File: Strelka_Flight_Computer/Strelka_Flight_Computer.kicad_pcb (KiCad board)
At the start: 4 copper layers, 91 x 30.1 mm, 170 parts, among them IC1 XTSD04GLGEAG, IC2 MAX-M10S-00B, J1 1S_LiPo_LARGE_HOLE_XT-30, J2 SM04B-GHS-TB(LF)(SN)-, J3 DB125-3.5-4P-GN-S, J4 SM06B-GHS-TB(LF)(SN), J6 USB_B_Micro, Q1 CJK2333, Q10 AP2300, Q11 MMBT2222, Q2 CJK2333, Q3 AO3401A, Q4 AO3401A, Q5 AP2300, Q6 MMBT2222, Q8 AO3401A, Q9 AO3401A, SW1 SW_Push, SW2 SW_Push, SW3 SM02B-GHS-TB(LF)(SN), U10 LM321, U11 BMX055, U12 MS561101BA03-50, U15 LM321, U16 TPS61085DGKR, U2 AP9101CK6, U3 AMS1117-3.3, U4 RFM95W-915S2, U5 STM32F405RGTx, U8 USBLC6-2SC6, Y1 Q13FC1350000200, Y2 X322524MOB4SI

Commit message: Started design for V2
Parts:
- removed C12: 0.1uF, Capacitor_SMD:C_0603_1608Metric_Pad1.08x0.95mm_HandSolder
- removed C13: 100nF, Capacitor_SMD:C_0603_1608Metric_Pad1.08x0.95mm_HandSolder
- removed C14, C16: 2.2uF, Capacitor_SMD:C_0603_1608Metric_Pad1.08x0.95mm_HandSolder
- removed C15: 10uF, Capacitor_SMD:C_0603_1608Metric_Pad1.08x0.95mm_HandSolder
- removed C17, C18: 10nF, Capacitor_SMD:C_0603_1608Metric_Pad1.08x0.95mm_HandSolder
- removed C19, C20: 8pF, Capacitor_SMD:C_0603_1608Metric_Pad1.08x0.95mm_HandSolder
- removed C2: 1u, Capacitor_SMD:C_0603_1608Metric
- removed C21, C22: 18pF, Capacitor_SMD:C_0603_1608Metric_Pad1.08x0.95mm_HandSolder
- removed C3: 10n, Capacitor_SMD:C_0603_1608Metric
- removed C4: 2.2u, Capacitor_SMD:C_0603_1608Metric
- removed C49, C50, C52, C53, C54: NC, Capacitor_SMD:C_0603_1608Metric
- removed D9: 1SS388, Diode_SMD:D_SOD-523
- removed FB1: BLM18PG221SN1D, Inductor_SMD:L_0603_1608Metric
- removed G***: LOGO, Footprints:Strelka_Logo
- removed G***: LOGO, Footprints:HPR_Logo
- removed I1, I2: AL5809-30S1-7, Diode_SMD:D_SOD-123
- removed J1: 1S_LiPo_LARGE_HOLE_XT-30, Connector_AMASS:AMASS_XT30PW-M_1x02_P2.50mm_Horizontal
- removed JP2: UART_Switch, Footprints:UART_Switch
- removed Q3, Q8: AO3401A, Package_TO_SOT_SMD:SOT-23
- removed R16, R17, R18, R19: 0, Resistor_SMD:R_0603_1608Metric_Pad0.98x0.95mm_HandSolder
- removed R22, R25: 10k, Resistor_SMD:R_0603_1608Metric_Pad0.98x0.95mm_HandSolder
- removed R28, R34, R48, R54: 1k, Resistor_SMD:R_0603_1608Metric
- removed R32, R52, R64, R69: 100k, Resistor_SMD:R_0603_1608Metric
- removed SW2: SW_Push, Button_Switch_SMD:SW_Push_SPST_NO_Alps_SKRK
- removed SW3: SM02B-GHS-TB(LF)(SN), Footprints:SM02BGHSTBLFSN
- removed U10, U15: LM321, Package_TO_SOT_SMD:SOT-23-5
- removed Y1: Q13FC1350000200, Crystal:Crystal_SMD_3215-2Pin_3.2x1.5mm
- removed Y2: X322524MOB4SI, Crystal:Crystal_SMD_3225-4Pin_3.2x2.5mm
- added BZ1: Buzzer, Footprints:HNB09A05, F.Cu at (102.3, 110.0)
- added C23: 100n, Capacitor_SMD:C_0402_1005Metric, F.Cu at (120.2, 107.8)
- added C24: 100n, Capacitor_SMD:C_0402_1005Metric, F.Cu at (120.2, 109.7)
- added C25: 100n, Capacitor_SMD:C_0402_1005Metric, F.Cu at (120.2, 111.7)
- added C32: 100n, Capacitor_SMD:C_0402_1005Metric, F.Cu at (120.2, 113.7)
- added C33: 100n, Capacitor_SMD:C_0402_1005Metric, F.Cu at (123.1, 105.8)
- added C34: 1u, Capacitor_SMD:C_0402_1005Metric, F.Cu at (123.1, 107.8)
- added C35: 2.2u, Capacitor_SMD:C_0402_1005Metric, F.Cu at (123.1, 109.7)
- added C42: 2.2u, Capacitor_SMD:C_0402_1005Metric, F.Cu at (123.1, 111.7)
- added C43: 100n, Capacitor_SMD:C_0402_1005Metric, F.Cu at (123.1, 113.7)
- added C44: 18p, Capacitor_SMD:C_0402_1005Metric, F.Cu at (125.9, 105.8)
- added C45: 18p, Capacitor_SMD:C_0402_1005Metric, F.Cu at (125.9, 107.8)
- added C5: 100n, Capacitor_SMD:C_0402_1005Metric, F.Cu at (120.2, 105.8)
- added C58: 18p, Capacitor_SMD:C_0402_1005Metric, F.Cu at (125.9, 109.7)
- added C59: 18p, Capacitor_SMD:C_0402_1005Metric, F.Cu at (125.9, 111.7)
- added D15: RED LED, LED_SMD:LED_0603_1608Metric, F.Cu at (126.7, 101.1)
- added D7: BLUE LED, LED_SMD:LED_0603_1608Metric, F.Cu at (126.7, 95.9)
- added D8: YELLOW LED, LED_SMD:LED_0603_1608Metric, F.Cu at (126.7, 98.5)
- added J5: Conn_01x07, Footprints:SM05B-GHS-TBLFSN, F.Cu at (189.1, 66.2)
- added J7: Conn_01x02, Footprints:MOLEX_43045-0200, F.Cu at (105.0, 52.0)
- added JP1: Jumper_2_Bridged, Jumper:SolderJumper-2_P1.3mm_Bridged_Pad1.0x1.5mm, F.Cu at (130.9, 96.4)
- added JP3: Jumper_2_Bridged, Jumper:SolderJumper-2_P1.3mm_Bridged_Pad1.0x1.5mm, F.Cu at (130.9, 99.9)
- added JP4: UART_Switch, Footprints:UART_Switch, F.Cu at (75.0, 158.0)
- added L1: 10u, Inductor_SMD:L_0805_2012Metric, F.Cu at (106.9, 116.6)
- added Q12: AO3400A, Package_TO_SOT_SMD:SOT-23, F.Cu at (129.8, 111.5)
- added Q13: AO3401A, Package_TO_SOT_SMD:SOT-23, F.Cu at (129.8, 115.9)
- added Q7: AO3400A, Package_TO_SOT_SMD:SOT-23, F.Cu at (129.8, 107.0)
- added R1: 100k, Resistor_SMD:R_0402_1005Metric, F.Cu at (111.5, 105.8)
- added R2: 1k, Resistor_SMD:R_0402_1005Metric, F.Cu at (111.5, 107.8)
- added R23: 1k, Resistor_SMD:R_0402_1005Metric, F.Cu at (114.4, 109.8)
- added R26: 10k, Resistor_SMD:R_0402_1005Metric, F.Cu at (114.4, 111.8)
- added R4: 10k, Resistor_SMD:R_0402_1005Metric, F.Cu at (111.5, 109.8)
- added R41: 0R, Resistor_SMD:R_0402_1005Metric, F.Cu at (114.4, 113.8)
- added R44: 10k, Resistor_SMD:R_0402_1005Metric, F.Cu at (117.3, 105.8)
- added R45: 10k, Resistor_SMD:R_0402_1005Metric, F.Cu at (117.3, 107.8)
- added R46: 1k, Resistor_SMD:R_0402_1005Metric, F.Cu at (117.3, 109.8)
- added R5: 33R, Resistor_SMD:R_0402_1005Metric, F.Cu at (111.5, 111.8)
- added R6: 1k, Resistor_SMD:R_0402_1005Metric, F.Cu at (111.5, 113.8)
- added R70: 100k, Resistor_SMD:R_0402_1005Metric, F.Cu at (117.3, 111.8)
- added R71: NC, Resistor_SMD:R_0603_1608Metric_Pad0.98x0.95mm_HandSolder, F.Cu at (112.2, 116.0)
- added R72: 10k, Resistor_SMD:R_0603_1608Metric_Pad0.98x0.95mm_HandSolder, F.Cu at (112.2, 118.5)
- added SW4: TS-1185-C-A-A-A, Button_Switch_SMD:SW_Push_SPST_NO_Alps_SKRK, F.Cu at (121.4, 96.8)
- added SW5: TS-1185-C-A-A-A, Button_Switch_SMD:SW_Push_SPST_NO_Alps_SKRK, F.Cu at (121.4, 101.3)
- added TP1: TestPoint, TestPoint:TestPoint_Pad_1.0x1.0mm, F.Cu at (95.9, 112.8)
- added TP11: TestPoint, TestPoint:TestPoint_Pad_1.0x1.0mm, F.Cu at (136.7, 162.2)
- added TP2: TestPoint, TestPoint:TestPoint_Pad_1.0x1.0mm, F.Cu at (127.5, 159.2)
- added U1: STM32F407VGTx, Package_QFP:LQFP-100_14x14mm_P0.5mm, F.Cu at (150.0, 66.2)
- added Y3: Q13FC1350000400, Crystal:Crystal_SMD_3215-2Pin_3.2x1.5mm, F.Cu at (140.5, 126.7)
- added Y4: X322524MOB4SI, Crystal:Crystal_SMD_3225-4Pin_3.2x2.5mm, F.Cu at (143.0, 130.5)
- AE1: footprint Connector_Coaxial:SMA_Amphenol_132134_Vertical -> Footprints:STA-10201
- AE2: footprint Connector_Coaxial:U.FL_Hirose_U.FL-R-SMT-1_Vertical -> Footprints:STA-10201
- BT2, C28, C29, C30, C31, C36, C38, C46, C47, C48, C51, C55, C56, C57, C6, D1, D11, D14, L2, MOSFET1, Q1, Q11, Q6, R27, R3, R30, R31, R35, R36, R37, R38, R39, R40, R47, R49, R53, R56, R61, R62, R63, R7, R9, U11, U12, U16, U2, U4, U8: moved to F.Cu
- C1: value 2.2u -> 100n; footprint Capacitor_SMD:C_0603_1608Metric -> Capacitor_SMD:C_0402_1005Metric
- D3: value E6X0602QBAC1UDA -> BZT52C3V6T; footprint LED_SMD:LED_0603_1608Metric_Pad1.05x0.95mm_HandSolder -> Diode_SMD:D_SOD-523
- D5: value 1SS388 -> BZT52C3V6T; moved to F.Cu
- J2: value SM04B-GHS-TB(LF)(SN)- -> Conn_01x04
- R10: value 10k -> 10R; footprint Resistor_SMD:R_0603_1608Metric -> Resistor_SMD:R_0402_1005Metric
- R11: footprint Resistor_SMD:R_0603_1608Metric -> Resistor_SMD:R_0402_1005Metric
- R12: value 10R -> 1k; footprint Resistor_SMD:R_0603_1608Metric -> Resistor_SMD:R_0402_1005Metric
- R13: value 200R -> 120R; footprint Resistor_SMD:R_0603_1608Metric_Pad0.98x0.95mm_HandSolder -> Resistor_SMD:R_0402_1005Metric
- R14, R15: value 0 -> 10k; footprint Resistor_SMD:R_0603_1608Metric_Pad0.98x0.95mm_HandSolder -> Resistor_SMD:R_0603_1608Metric; moved to F.Cu
- R21: value 10k -> 1k; footprint Resistor_SMD:R_0603_1608Metric_Pad0.98x0.95mm_HandSolder -> Resistor_SMD:R_0603_1608Metric; moved to F.Cu
- R24: value NC -> 1k; footprint Resistor_SMD:R_0603_1608Metric_Pad0.98x0.95mm_HandSolder -> Resistor_SMD:R_0603_1608Metric
- SW1: value SW_Push -> SW_DIP_x01; footprint Button_Switch_SMD:SW_Push_SPST_NO_Alps_SKRK -> Footprints:MOLEX_43045-0200
- U5: value STM32F405RGTx -> MCP2551-I-SN; footprint Package_QFP:LQFP-64_10x10mm_P0.5mm -> Package_SO:SOIC-8_3.9x4.9mm_P1.27mm
- moved J2 135.8 mm to (63.4, 156.9), turned to 0 degrees
- moved J6 131.1 mm to (63.3, 162.9), turned to 0 degrees
- moved U8 116.6 mm to (70.9, 154.7), turned to 0 degrees
- moved R12 109.7 mm to (75.0, 153.5), turned to 0 degrees
- moved U5 109.1 mm to (72.4, 163.1)
- moved R56 108.5 mm to (81.9, 134.8)
- moved C39 105.3 mm to (81.9, 129.8), turned to 0 degrees
- moved C40 104.8 mm to (81.9, 132.3), turned to 0 degrees
- moved C38 104.6 mm to (81.9, 127.3)
- moved BT2 104.3 mm to (88.1, 140.9), turned to 0 degrees
- moved R58 100.9 mm to (81.9, 139.9), turned to 0 degrees
- moved C11 100.8 mm to (69.9, 144.9), turned to 0 degrees
- moved R57 98.4 mm to (81.9, 137.3), turned to 0 degrees
- moved R40 98.3 mm to (108.4, 163.9), turned to 0 degrees
- moved C10 97.9 mm to (69.9, 142.3), turned to 0 degrees
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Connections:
- C1 pad 1: GND -> +5V
- C1 pad 2: Net-(C1-Pad2) -> GND
- D1 pad 1: Net-(D1-Pad1) -> Net-(D1-K)
- D3 pad 1: Net-(D3-Pad1) -> /Actuators/DROGUE_CONT
- D3 pad 2: /STM32F405/INDICATOR_LED -> GND
- D5 pad 1: /Actuators/Ematch_Drogue1/EMATCH+ -> /Actuators/MAIN_CONT
- D5 pad 2: Net-(D5-Pad2) -> GND
- IC2 pad 16: /STM32F405/I2C2_SDA -> /STM32F407/I2C2_SDA
- IC2 pad 17: /STM32F405/I2C2_SCL -> /STM32F407/I2C2_SCL
- IC2 pad 2: Net-(IC2-Pad2) -> /STM32F407/USART2_RX
- IC2 pad 3: Net-(IC2-Pad3) -> /STM32F407/USART2_TX
- IC2 pad 9: /STM32F405/GPIO_PA10 -> /STM32F407/GPIO_PA10
- J2 pad 1: /Data_Interfaces/SWCLK -> GND
- J2 pad 2: /Data_Interfaces/SWDIO -> /Data_Interfaces/CAN_+
- J2 pad 3: GND -> /Data_Interfaces/CAN_-
- J2 pad 4: +3V3 -> GND
- J2 pad SH1: GND -> (no net)
- J2 pad SH2: GND -> (no net)
- Q1 pad 2: Net-(D1-Pad1) -> Net-(D1-K)
- R10 pad 1: Net-(R10-Pad1) -> Net-(U1-PB14)
- R10 pad 2: GND -> /Data_Interfaces/USB_D-
- R11 pad 1: /Data_Interfaces/USB_D- -> Net-(U1-PB15)
- R11 pad 2: /STM32F405/USB2_IN- -> /Data_Interfaces/USB_D+
- R12 pad 1: /Data_Interfaces/USB_D+ -> Net-(U5-Rs)
- R12 pad 2: /STM32F405/USB2_IN+ -> GND
- R13 pad 1: GND -> /Data_Interfaces/CAN_+
- R13 pad 2: Net-(D3-Pad1) -> /Data_Interfaces/CAN_-
- R14 pad 1: /Data_Logging/SD0 -> /Actuators/DROGUE_CONT
- R14 pad 2: /STM32F405/SDIO_D0 -> /Actuators/Ematch_Drogue1/EMATCH+
- R15 pad 1: /Data_Logging/SD1 -> /Actuators/MAIN_CONT
- R15 pad 2: /STM32F405/SDIO_D1 -> /Actuators/Ematch_Main/EMATCH+
- R21 pad 1: /STM32F405/I2C2_SDA -> /Actuators/Ematch_Drogue1/EMATCH+
- R21 pad 2: +3V3 -> VDC
- R24 pad 1: /STM32F405/SD_DET -> /Actuators/Ematch_Main/EMATCH+
- R24 pad 2: +3V3 -> VDC
- R58 pad 2: /STM32F405/GPIO_PB7 -> /STM32F407/GPIO_PB7
- SW1 pad 1: +3V3 -> Net-(D1-K)
- SW1 pad 2: Net-(R10-Pad1) -> VDC
- TP10 pad 1: /STM32F405/USART2_TX -> /STM32F407/USART2_TX
- TP5 pad 1: /Actuators/DROGUE_CONT -> /STM32F407/SPI2_NSS3
- TP6 pad 1: /STM32F405/SPI2_MOSI -> /915MHz_Radio/SPI_MOSI
- TP7 pad 1: /STM32F405/SPI2_MISO -> /915MHz_Radio/SPI_MISO
- TP8 pad 1: /STM32F405/SPI2_SCK -> /915MHz_Radio/SPI_CLK
- TP9 pad 1: /STM32F405/USART2_RX -> /STM32F407/USART2_RX
- U11 pad 11: /STM32F405/SPI2_MOSI -> /915MHz_Radio/SPI_MOSI
- U11 pad 12: /STM32F405/SPI2_MISO -> /915MHz_Radio/SPI_MISO
- U11 pad 14: /STM32F405/INT_IN2 -> /STM32F407/INT_IN2
- U11 pad 16: /STM32F405/SPI2_NSS2 -> /STM32F407/SPI2_NSS2
- U11 pad 17: /STM32F405/SPI2_MISO -> /915MHz_Radio/SPI_MISO
- U11 pad 19: /STM32F405/INT_IN1 -> /STM32F407/INT_IN1
- U11 pad 2: /STM32F405/INT_IN3 -> /STM32F407/INT_IN3
- U11 pad 20: /STM32F405/SPI2_NSS4 -> /STM32F407/SPI2_NSS4
- U11 pad 5: /STM32F405/SPI2_NSS3 -> /STM32F407/SPI2_NSS3
- U11 pad 9: /STM32F405/SPI2_SCK -> /915MHz_Radio/SPI_CLK
- U12 pad 4: /STM32F405/SPI2_NSS1 -> /STM32F407/SPI2_NSS1
- U12 pad 5: /STM32F405/SPI2_NSS1 -> /STM32F407/SPI2_NSS1
- U12 pad 6: /STM32F405/SPI2_MISO -> /STM32F407/SPI2_MISO
- U12 pad 7: /STM32F405/SPI2_MOSI -> /STM32F407/SPI2_MOSI
- U12 pad 8: /STM32F405/SPI2_SCK -> /STM32F407/SPI2_SCK
- U5 pad 1: +3V3 -> Net-(JP4-RX1)
- U5 pad 2: /Actuators/CONT_TEST_EN -> GND
- U5 pad 3: /STM32F405/OSC32_IN -> +5V
- U5 pad 4: /STM32F405/OSC32_OUT -> Net-(JP4-TX1)
- U5 pad 5: /STM32F405/OSC_IN -> unconnected-(U5-Vref-Pad5)
- U5 pad 6: /STM32F405/OSC_OUT -> /Data_Interfaces/CAN_-
- U5 pad 7: Net-(C12-Pad2) -> /Data_Interfaces/CAN_+
- U5 pad 8: /Power/BATT_VOLT -> Net-(U5-Rs)
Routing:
- net +3V3: track 159.9 -> 0.00 mm, vias 41 -> 0
- net GND: track 102.2 -> 0.00 mm, vias 48 -> 0
- net VDC: track 90.5 -> 0.00 mm, vias 5 -> 0
- net /Actuators/CONT_TEST_EN: track 66.1 -> 0.00 mm, vias 5 -> 0
- net VBUS: track 64.9 -> 0.00 mm, vias 3 -> 0
- net /Actuators/DROGUE_CONT: track 62.4 -> 0.00 mm, vias 2 -> 0
- net Net-(C12-Pad2): track 56.9 -> 0.00 mm, vias 2 -> 0
- net /Actuators/MAIN_CONT: track 55.8 -> 0.00 mm, vias 2 -> 0
- net /Actuators/DROGUE_L: track 54.0 -> 0.00 mm, vias 4 -> 0
- net /STM32F405/USART2_TX: track 50.7 -> 0.00 mm, vias 2 -> 0
- net /STM32F405/SPI2_MISO: track 50.4 -> 0.00 mm, vias 5 -> 0
- net /Data_Interfaces/SWCLK: track 48.5 -> 0.00 mm, vias 2 -> 0
- net /STM32F405/SPI2_MOSI: track 46.1 -> 0.00 mm, vias 5 -> 0
- net Net-(R10-Pad1): track 45.4 -> 0.00 mm, vias 2 -> 0
- net /Actuators/MAIN_L: track 44.5 -> 0.00 mm, vias 4 -> 0
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- removed copper zone on F.Cu, net +3V3
- removed copper zone on In2.Cu, net +3V3
- removed copper zone on B.Cu, net GND
- removed copper zone on F.Cu, net GND
- removed copper zone on In1.Cu, net GND
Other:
- board size 91 x 30.1 mm -> 93.7 x 35.8 mm
- board text removed: "+"
- board text removed: "+3.3V"
- board text removed: "+5V"
- board text removed: "-"
- board text removed: "4.2Vin MAX"
- board text removed: "BOOT"
- board text removed: "Batt PWR Select"
- board text removed: "DROGUE"
- board text removed: "Designed by Angus McLennan Nov 2022"
- board text removed: "GPS"
- board text removed: "JLCJLCJLC"
- board text removed: "MAIN"
- board text removed: "MISO"
- board text removed: "MOSI"
- board text removed: "MS5611"
- board text removed: "PWR SW"
- board text removed: "RST"
- board text removed: "RX2"
- board text removed: "SCK"
- board text removed: "SWD"
- board text removed: "TX2"
- board text removed: "UART SW"

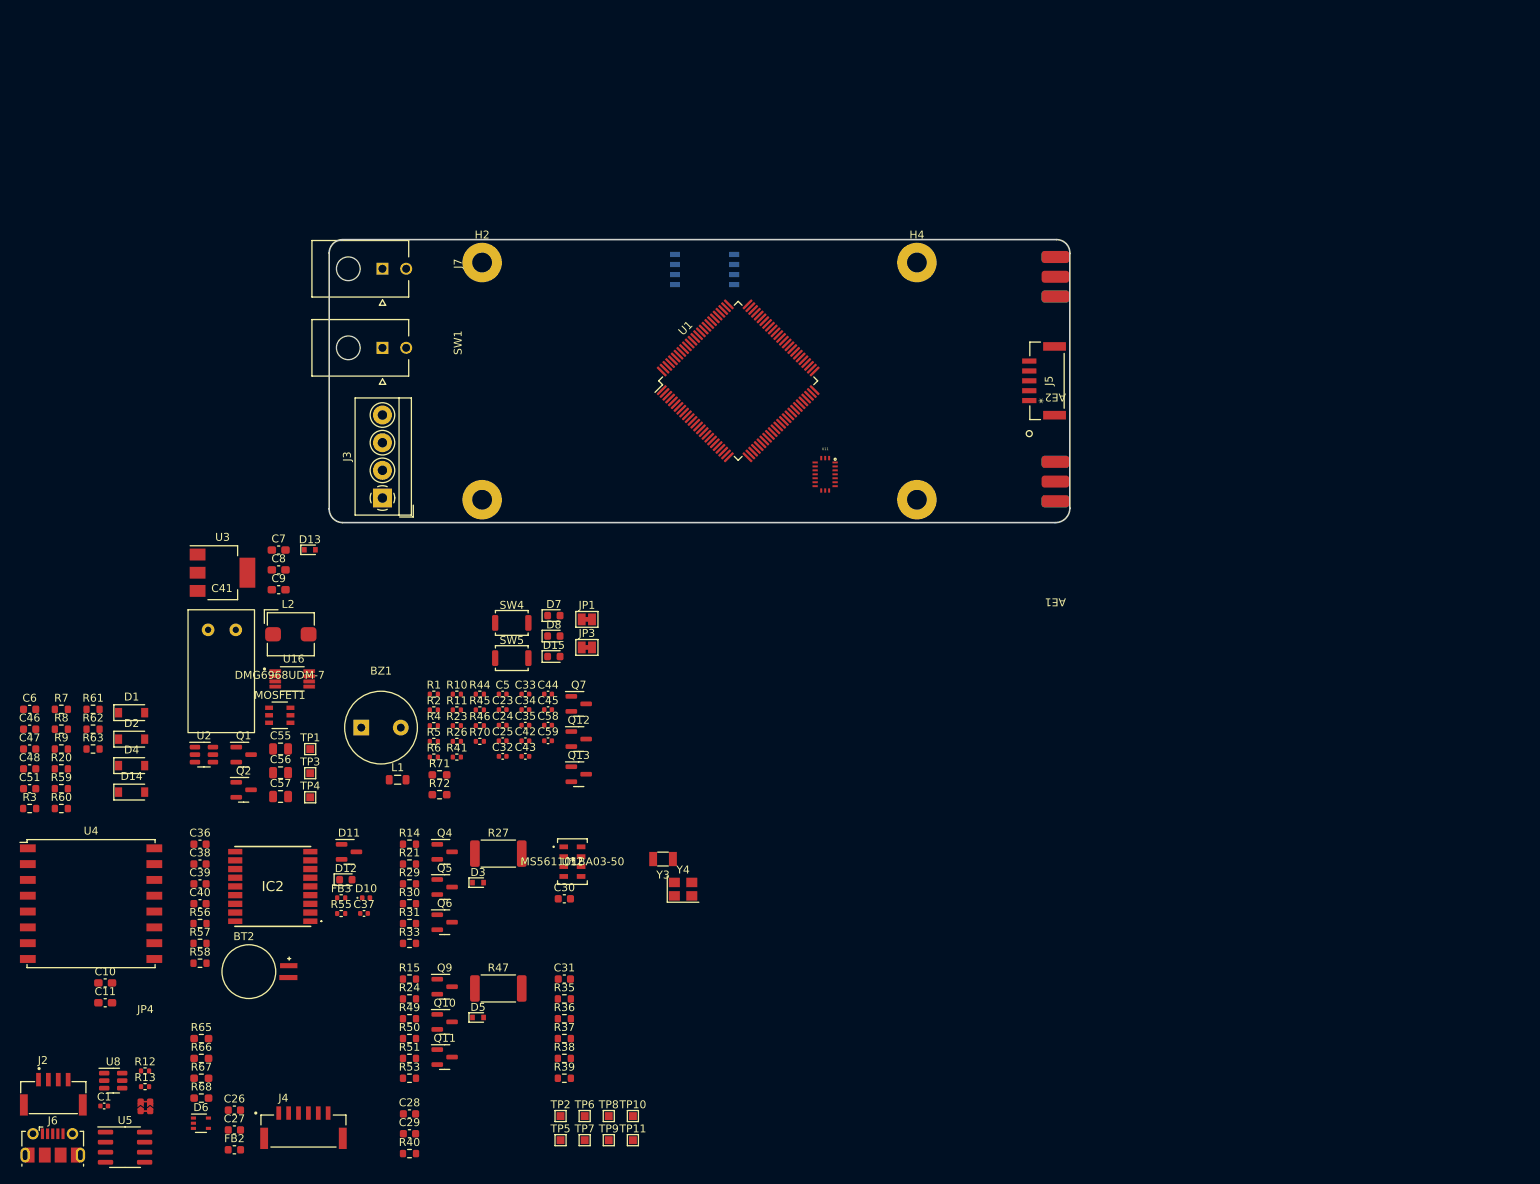
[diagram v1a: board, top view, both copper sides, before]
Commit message: Changes main processor to h4745
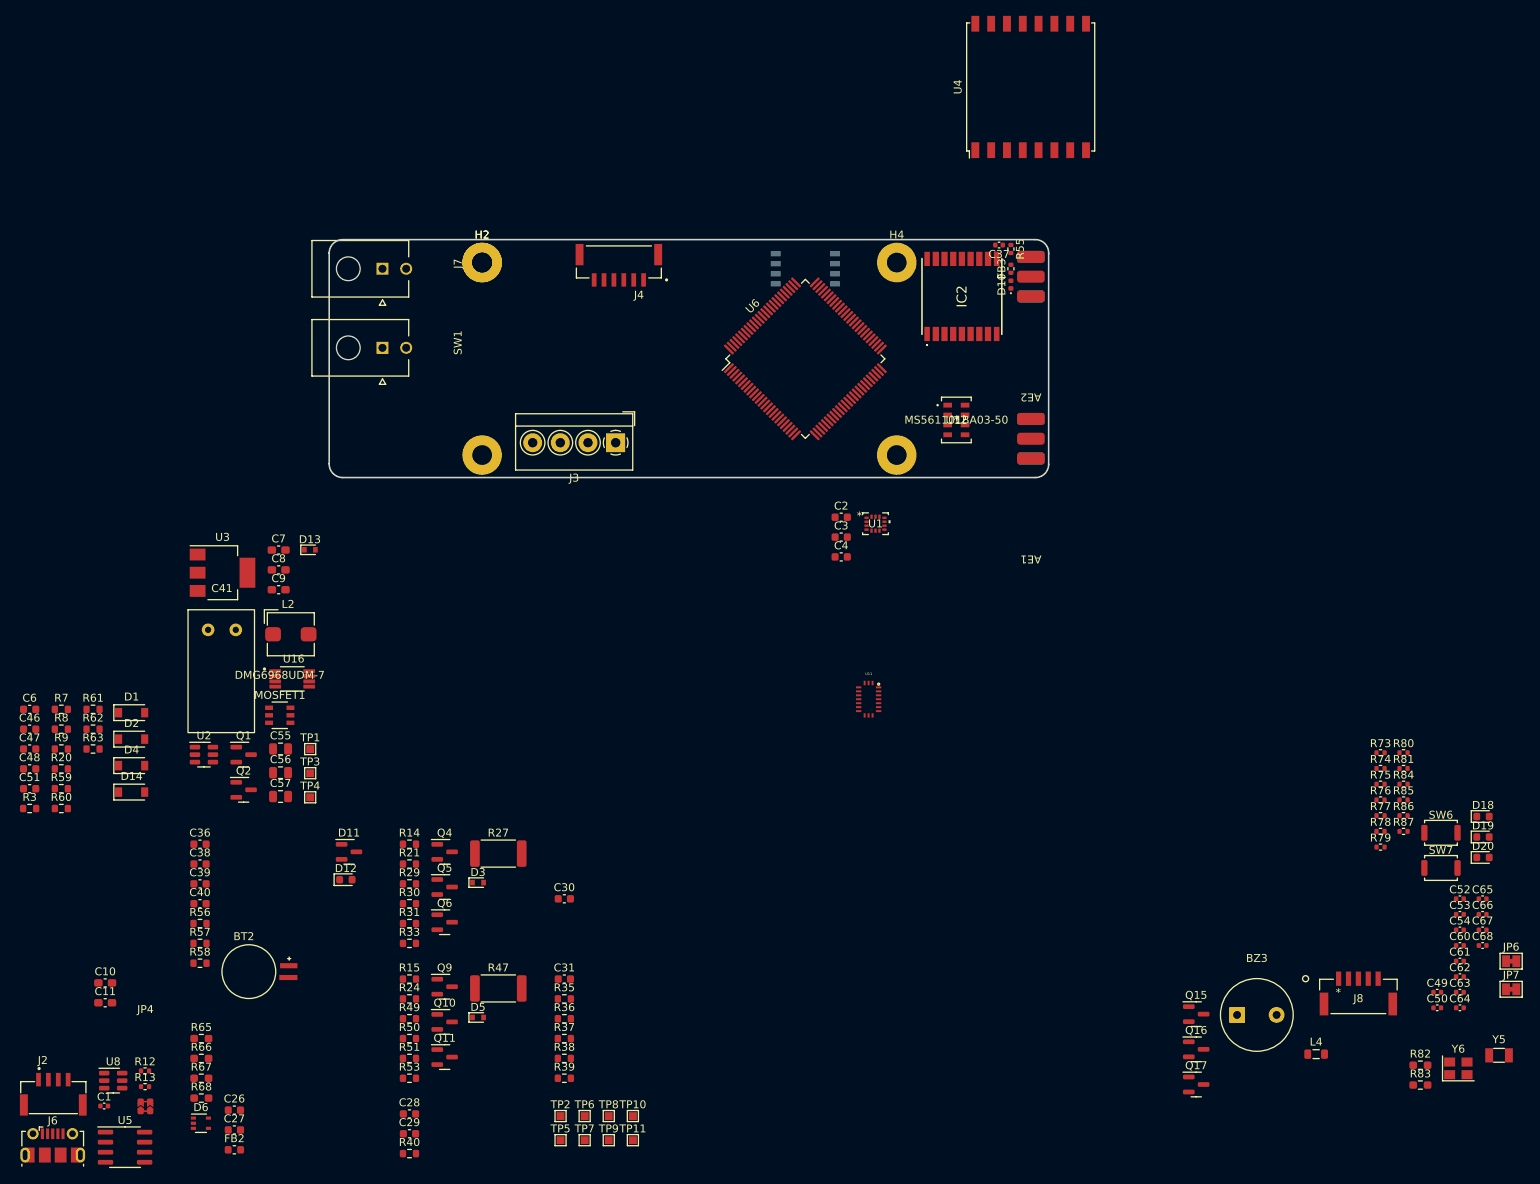
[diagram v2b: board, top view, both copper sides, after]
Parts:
- removed BZ1: Buzzer, Footprints:HNB09A05
- removed C23, C24, C25, C32, C33, C43, C5: 100n, Capacitor_SMD:C_0402_1005Metric
- removed C34: 1u, Capacitor_SMD:C_0402_1005Metric
- removed C35, C42: 2.2u, Capacitor_SMD:C_0402_1005Metric
- removed C44, C45, C58, C59: 18p, Capacitor_SMD:C_0402_1005Metric
- removed D15: RED LED, LED_SMD:LED_0603_1608Metric
- removed D7: BLUE LED, LED_SMD:LED_0603_1608Metric
- removed D8: YELLOW LED, LED_SMD:LED_0603_1608Metric
- removed J5: Conn_01x07, Footprints:SM05B-GHS-TBLFSN
- removed JP1, JP3: Jumper_2_Bridged, Jumper:SolderJumper-2_P1.3mm_Bridged_Pad1.0x1.5mm
- removed L1: 10u, Inductor_SMD:L_0805_2012Metric
- removed Q12, Q7: AO3400A, Package_TO_SOT_SMD:SOT-23
- removed Q13: AO3401A, Package_TO_SOT_SMD:SOT-23
- removed R1, R70: 100k, Resistor_SMD:R_0402_1005Metric
- removed R10, R11: 10R, Resistor_SMD:R_0402_1005Metric
- removed R2, R23, R46, R6: 1k, Resistor_SMD:R_0402_1005Metric
- removed R26, R4, R44, R45: 10k, Resistor_SMD:R_0402_1005Metric
- removed R41: 0R, Resistor_SMD:R_0402_1005Metric
- removed R5: 33R, Resistor_SMD:R_0402_1005Metric
- removed R71: NC, Resistor_SMD:R_0603_1608Metric_Pad0.98x0.95mm_HandSolder
- removed R72: 10k, Resistor_SMD:R_0603_1608Metric_Pad0.98x0.95mm_HandSolder
- removed SW4, SW5: TS-1185-C-A-A-A, Button_Switch_SMD:SW_Push_SPST_NO_Alps_SKRK
- removed Y3: Q13FC1350000400, Crystal:Crystal_SMD_3215-2Pin_3.2x1.5mm
- removed Y4: X322524MOB4SI, Crystal:Crystal_SMD_3225-4Pin_3.2x2.5mm
- added BZ3: Buzzer, Footprints:HNB09A05, F.Cu at (213.1, 146.4)
- added C2: 100nF, Capacitor_SMD:C_0603_1608Metric, F.Cu at (163.0, 83.4)
- added C3: 10uF, Capacitor_SMD:C_0603_1608Metric, F.Cu at (163.0, 85.9)
- added C4: 100nF, Capacitor_SMD:C_0603_1608Metric, F.Cu at (163.0, 88.5)
- added C49: 1u, Capacitor_SMD:C_0402_1005Metric, F.Cu at (238.4, 143.5)
- added C50: 100n, Capacitor_SMD:C_0402_1005Metric, F.Cu at (238.4, 145.5)
- added C52: 100n, Capacitor_SMD:C_0402_1005Metric, F.Cu at (241.3, 131.7)
- added C53: 100n, Capacitor_SMD:C_0402_1005Metric, F.Cu at (241.3, 133.7)
- added C54: 100n, Capacitor_SMD:C_0402_1005Metric, F.Cu at (241.3, 135.6)
- added C60: 100n, Capacitor_SMD:C_0402_1005Metric, F.Cu at (241.3, 137.6)
- added C61: 100n, Capacitor_SMD:C_0402_1005Metric, F.Cu at (241.3, 139.6)
- added C62: 18p, Capacitor_SMD:C_0402_1005Metric, F.Cu at (241.3, 141.6)
- added C63: 18p, Capacitor_SMD:C_0402_1005Metric, F.Cu at (241.3, 143.5)
- added C64: 15p, Capacitor_SMD:C_0402_1005Metric, F.Cu at (241.3, 145.5)
- added C65: 15p, Capacitor_SMD:C_0402_1005Metric, F.Cu at (244.2, 131.7)
- added C66: 100n, Capacitor_SMD:C_0402_1005Metric, F.Cu at (244.2, 133.7)
- added C67: 2.2u, Capacitor_SMD:C_0402_1005Metric, F.Cu at (244.2, 135.6)
- added C68: 2.2u, Capacitor_SMD:C_0402_1005Metric, F.Cu at (244.2, 137.6)
- added D18: BLUE LED, LED_SMD:LED_0603_1608Metric, F.Cu at (244.2, 121.3)
- added D19: YELLOW LED, LED_SMD:LED_0603_1608Metric, F.Cu at (244.2, 123.9)
- added D20: RED LED, LED_SMD:LED_0603_1608Metric, F.Cu at (244.2, 126.5)
- added H2: MountingHole, MountingHole:MountingHole_2.5mm_Pad, F.Cu at (117.6, 51.2)
- added J8: Conn_01x07, Footprints:SM05B-GHS-TBLFSN, F.Cu at (228.5, 144.1)
- added JP6: Jumper_2_Bridged, Jumper:SolderJumper-2_P1.3mm_Bridged_Pad1.0x1.5mm, F.Cu at (247.8, 139.6)
- added JP7: Jumper_2_Bridged, Jumper:SolderJumper-2_P1.3mm_Bridged_Pad1.0x1.5mm, F.Cu at (247.8, 143.1)
- added L4: 10u, Inductor_SMD:L_0805_2012Metric, F.Cu at (223.1, 151.3)
- added Q15: AO3400A, Package_TO_SOT_SMD:SOT-23, F.Cu at (207.9, 146.3)
- added Q16: AO3400A, Package_TO_SOT_SMD:SOT-23, F.Cu at (207.9, 150.7)
- added Q17: AO3401A, Package_TO_SOT_SMD:SOT-23, F.Cu at (207.9, 155.2)
- added R73: 100k, Resistor_SMD:R_0402_1005Metric, F.Cu at (231.3, 113.2)
- added R74: 1k, Resistor_SMD:R_0402_1005Metric, F.Cu at (231.3, 115.2)
- added R75: 10k, Resistor_SMD:R_0402_1005Metric, F.Cu at (231.3, 117.2)
- added R76: 33R, Resistor_SMD:R_0402_1005Metric, F.Cu at (231.3, 119.2)
- added R77: 1k, Resistor_SMD:R_0402_1005Metric, F.Cu at (231.3, 121.2)
- added R78: 1k, Resistor_SMD:R_0402_1005Metric, F.Cu at (231.3, 123.2)
- added R79: 10k, Resistor_SMD:R_0402_1005Metric, F.Cu at (231.3, 125.2)
- added R80: 1k, Resistor_SMD:R_0402_1005Metric, F.Cu at (234.2, 113.2)
- added R81: 100k, Resistor_SMD:R_0402_1005Metric, F.Cu at (234.2, 115.2)
- added R82: NC, Resistor_SMD:R_0603_1608Metric_Pad0.98x0.95mm_HandSolder, F.Cu at (236.3, 152.8)
- added R83: 10k, Resistor_SMD:R_0603_1608Metric_Pad0.98x0.95mm_HandSolder, F.Cu at (236.3, 155.3)
- added R84: 10R, Resistor_SMD:R_0402_1005Metric, F.Cu at (234.2, 117.2)
- added R85: 10R, Resistor_SMD:R_0402_1005Metric, F.Cu at (234.2, 119.2)
- added R86: 10k, Resistor_SMD:R_0402_1005Metric, F.Cu at (234.2, 121.2)
- added R87: 10k, Resistor_SMD:R_0402_1005Metric, F.Cu at (234.2, 123.2)
- added SW6: TS-1185-C-A-A-A, Button_Switch_SMD:SW_Push_SPST_NO_Alps_SKRK, F.Cu at (238.9, 123.3)
- added SW7: TS-1185-C-A-A-A, Button_Switch_SMD:SW_Push_SPST_NO_Alps_SKRK, F.Cu at (238.9, 127.8)
- added U6: STM32H743VITx, Package_QFP:LQFP-100_14x14mm_P0.5mm, F.Cu at (158.5, 63.4)
- added Y5: Q13FC1350000400, Crystal:Crystal_SMD_3215-2Pin_3.2x1.5mm, F.Cu at (246.2, 151.5)
- added Y6: X1E0000210834, Crystal:Crystal_SMD_SeikoEpson_TSX3225-4Pin_3.2x2.5mm, F.Cu at (241.1, 153.2)
- U1: value STM32F407VGTx -> ASM330LHHXTR; footprint Package_QFP:LQFP-100_14x14mm_P0.5mm -> Footprints:QFN_LHHXTR_STM
- moved U4 157.5 mm to (187.0, 29.0), turned to 90 degrees
- moved R55 119.3 mm to (184.5, 49.5), turned to -90 degrees
- moved C37 116.6 mm to (183.0, 49.0), turned to 180 degrees
- moved FB3 116.2 mm to (184.5, 52.0), turned to 90 degrees
- moved J4 116.2 mm to (134.9, 51.5), turned to 180 degrees
- moved IC2 114.8 mm to (178.3, 55.5), turned to -90 degrees
- moved D10 112.6 mm to (184.5, 54.0), turned to 90 degrees
- moved U12 74.0 mm to (177.6, 71.1)
- moved J3 30.3 mm to (134.5, 74.0), turned to 180 degrees
- moved U11 29.0 mm to (166.5, 106.5)
- moved U1 25.1 mm to (167.4, 84.2), turned to 0 degrees
- moved IC1 12.8 mm to (158.5, 52.0), turned to 0 degrees
- moved AE1 6.24 mm to (187.0, 73.5)
- moved H1 6.19 mm to (170.1, 75.6)
- moved H3 5.64 mm to (117.6, 75.6)
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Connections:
- IC2 pad 16: /STM32F407/I2C2_SDA -> /STM32H743/I2C2_SDA
- IC2 pad 17: /STM32F407/I2C2_SCL -> /STM32H743/I2C2_SCL
- IC2 pad 2: /STM32F407/USART2_RX -> /STM32H743/USART2_RX
- IC2 pad 3: /STM32F407/USART2_TX -> /STM32H743/USART2_TX
- IC2 pad 9: /STM32F407/GPIO_PA10 -> /STM32H743/GPS_RST
- R58 pad 2: /STM32F407/GPIO_PB7 -> /STM32H743/GPS_PPS
- TP10 pad 1: /STM32F407/USART2_TX -> /STM32H743/USART2_TX
- TP11 pad 1: /STM32F407/SPI2_NSS4 -> /STM32H743/SPI2_NSS3
- TP2 pad 1: /STM32F407/SPI2_NSS2 -> /STM32H743/SPI2_NSS1
- TP5 pad 1: /STM32F407/SPI2_NSS3 -> /STM32H743/SPI2_NSS2
- TP9 pad 1: /STM32F407/USART2_RX -> /STM32H743/USART2_RX
- U1 pad 1: unconnected-(U1-PE2-Pad1) -> /915MHz_Radio/SPI_MISO
- U1 pad 10: GND -> unconnected-(U1-NC-Pad10)
- U1 pad 11: +3.3V -> unconnected-(U1-NC-Pad11)
- U1 pad 12: /STM32F407/OSC_IN -> /STM32H743/SPI2_NSS4
- U1 pad 13: /STM32F407/OSC_OUT -> /915MHz_Radio/SPI_CLK
- U1 pad 14: /STM32F407/NRST -> /915MHz_Radio/SPI_MOSI
- U1 pad 2: unconnected-(U1-PE3-Pad2) -> GND
- U1 pad 3: unconnected-(U1-PE4-Pad3) -> GND
- U1 pad 4: unconnected-(U1-PE5-Pad4) -> /STM32H743/INT_IN4
- U1 pad 5: unconnected-(U1-PE6-Pad5) -> +3V3
- U1 pad 6: Net-(U1-VBAT) -> unconnected-(U1-NC-Pad6)
- U1 pad 7: unconnected-(U1-PC13-Pad7) -> GND
- U1 pad 8: /STM32F407/OSC32_IN -> +3V3
- U1 pad 9: /STM32F407/OSC32_OUT -> /STM32H743/INT_IN5
- U11 pad 14: /STM32F407/INT_IN2 -> /STM32H743/INT_IN2
- U11 pad 16: /STM32F407/SPI2_NSS2 -> /STM32H743/SPI2_NSS1
- U11 pad 19: /STM32F407/INT_IN1 -> /STM32H743/INT_IN1
- U11 pad 2: /STM32F407/INT_IN3 -> /STM32H743/INT_IN3
- U11 pad 20: /STM32F407/SPI2_NSS4 -> /STM32H743/SPI2_NSS3
- U11 pad 5: /STM32F407/SPI2_NSS3 -> /STM32H743/SPI2_NSS2
- U12 pad 4: /STM32F407/SPI2_NSS1 -> /STM32H743/SPI4_NSS
- U12 pad 5: /STM32F407/SPI2_NSS1 -> /STM32H743/SPI4_NSS
- U12 pad 6: /STM32F407/SPI2_MISO -> /STM32H743/SPI4_MISO
- U12 pad 7: /STM32F407/SPI2_MOSI -> /STM32H743/SPI4_MOSI
- U12 pad 8: /STM32F407/SPI2_SCK -> /STM32H743/SPI4_SCK
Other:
- board size 93.7 x 35.8 mm -> 91 x 30.1 mm
